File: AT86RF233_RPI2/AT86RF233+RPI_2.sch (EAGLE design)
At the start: 6 parts, among them U1 ATZB-RF-233-1-C

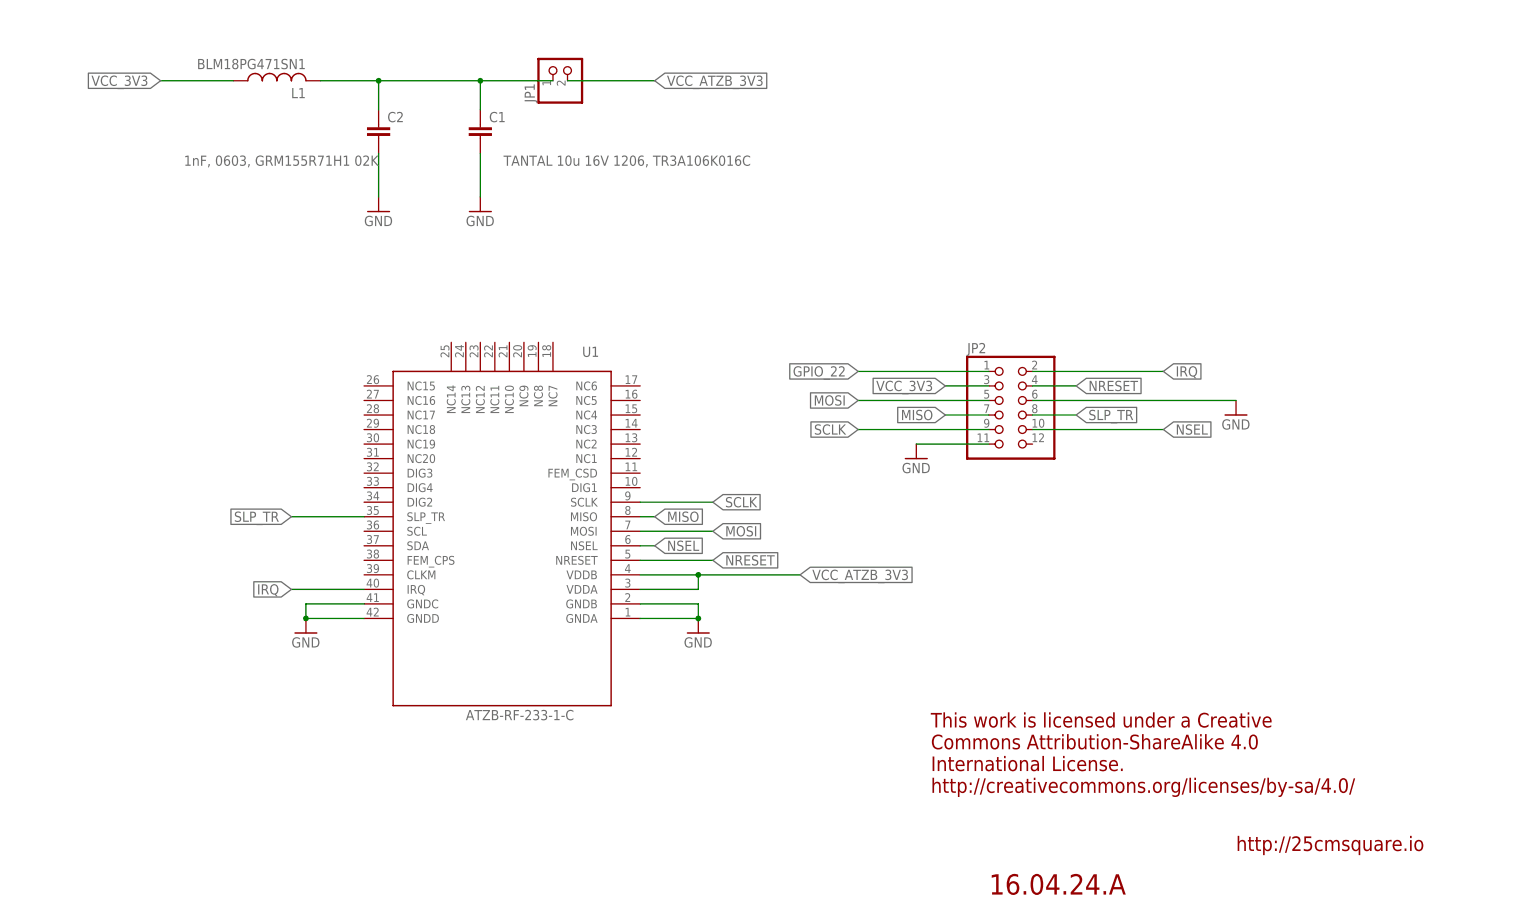
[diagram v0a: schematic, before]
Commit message: at86rf233: added reset switch
Signed-off-by: malo <malo@25cmsquare.io>
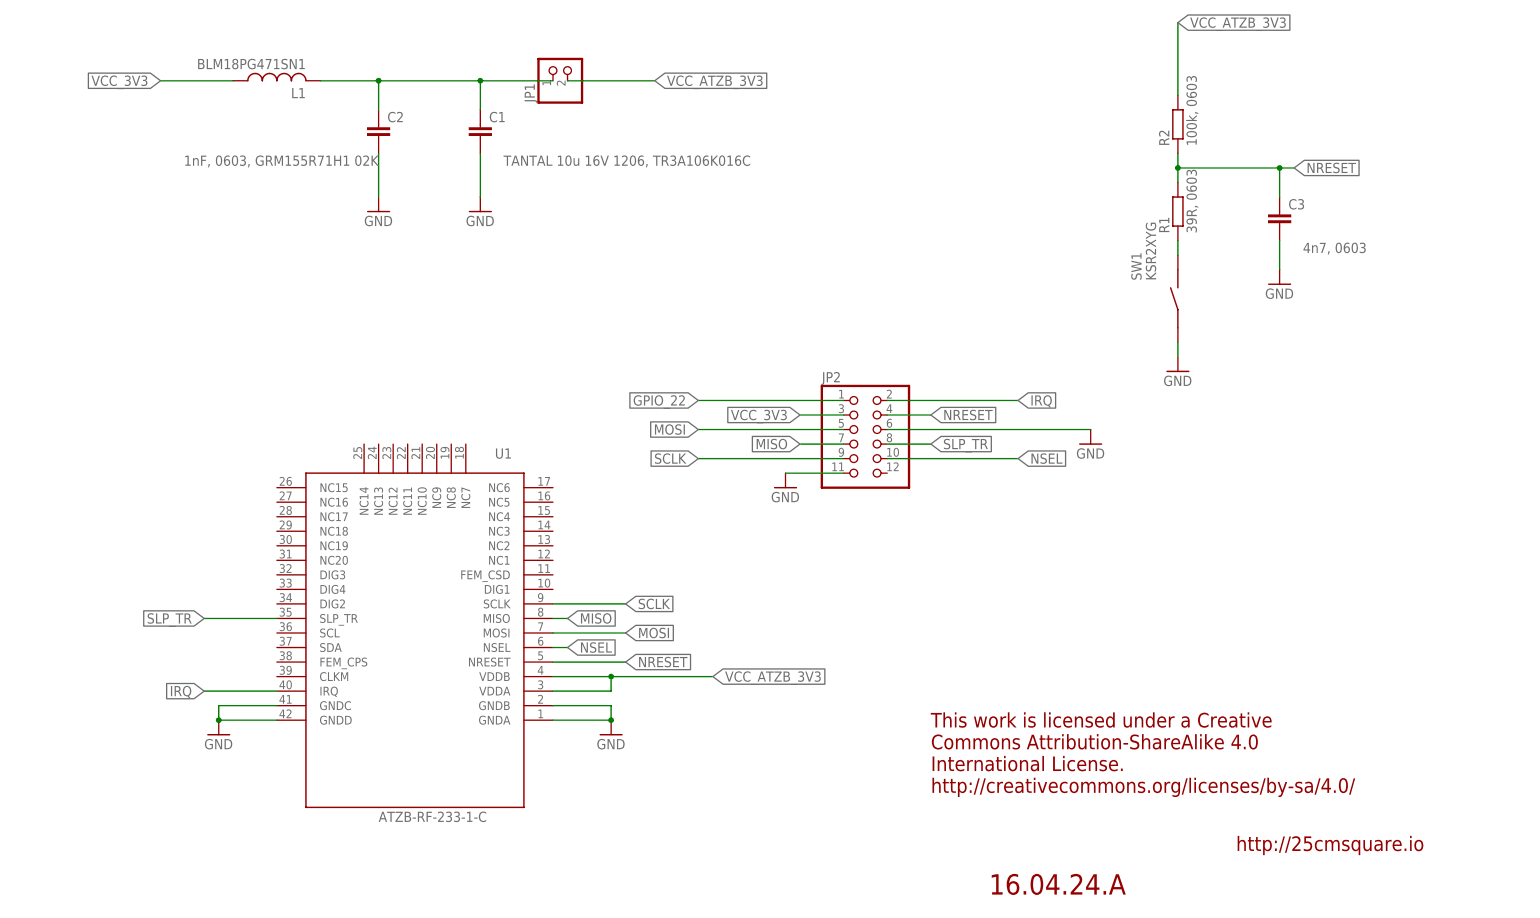
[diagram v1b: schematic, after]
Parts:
- added C3: 4n7, 0603, rcl:C-EUC0603K
- added R1: 39R, 0603, resistor:R-EU_R0603
- added R2: 100k, 0603, resistor:R-EU_R0603
- added SW1: KSR2XYG, 25cmsquare:KSR2XYG
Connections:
- new net N$1: R1.1, SW1.1
- net GND: now also C3.2, SW1.2
- net NRESET: now also C3.1, R1.2, R2.1
- net VCC_ATZB_3V3: now also R2.2
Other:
- moved on the sheet: JP2, U1

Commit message: at86rf233: board created
Signed-off-by: malo <malo@25cmsquare.io>
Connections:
- removed net N$2: C1.1, C2.1, JP1.1, L1.2
- new net N$3: JP1.2, L1.1
- net VCC_3V3: now also JP1.1; no longer L1.1
- net VCC_ATZB_3V3: now also C1.1, C2.1, L1.2; no longer JP1.2
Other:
- moved on the sheet: JP1
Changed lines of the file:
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@@
 <?xml version="1.0" encoding="utf-8"?>
 <!DOCTYPE eagle SYSTEM "eagle.dtd">
-<eagle version="7.2.0">
+<eagle version="7.5.0">
 <drawing>
 <settings>
@@
 </instance>
 <instance part="GND1" gate="1" x="83.82" y="132.08"/>
-<instance part="JP1" gate="G$1" x="99.06" y="157.48" rot="R90"/>
+<instance part="JP1" gate="G$1" x="27.94" y="157.48" rot="R90"/>
 <instance part="GND2" gate="1" x="38.1" y="40.64"/>
 <instance part="GND3" gate="1" x="106.68" y="40.64"/>
@@
 <net name="VCC_3V3" class="0">
 <segment>
-<pinref part="L1" gate="G$1" pin="1"/>
-<wire x1="40.64" y1="154.94" x2="27.94" y2="154.94" width="0.1524" layer="91"/>
-<label x="27.94" y="154.94" size="1.778" layer="95" rot="R180" xref="yes"/>
+<wire x1="25.4" y1="154.94" x2="17.78" y2="154.94" width="0.1524" layer="91"/>
+<label x="17.78" y="154.94" size="1.778" layer="95" rot="R180" xref="yes"/>
+<pinref part="JP1" gate="G$1" pin="1"/>
 </segment>
 <segment>
@@
 </segment>
 </net>
-<net name="N$2" class="0">
-<segment>
+<net name="VCC_ATZB_3V3" class="0">
+<segment>
+<label x="114.3" y="154.94" size="1.778" layer="95" xref="yes"/>
 <pinref part="L1" gate="G$1" pin="2"/>
-<pinref part="JP1" gate="G$1" pin="1"/>
 <wire x1="55.88" y1="154.94" x2="66.04" y2="154.94" width="0.1524" layer="91"/>
 <pinref part="C2" gate="G$1" pin="1"/>
 <wire x1="66.04" y1="154.94" x2="83.82" y2="154.94" width="0.1524" layer="91"/>
-<wire x1="83.82" y1="154.94" x2="96.52" y2="154.94" width="0.1524" layer="91"/>
 <wire x1="66.04" y1="149.86" x2="66.04" y2="154.94" width="0.1524" layer="91"/>
 <junction x="66.04" y="154.94"/>
 <pinref part="C1" gate="G$1" pin="1"/>
 <wire x1="83.82" y1="149.86" x2="83.82" y2="154.94" width="0.1524" layer="91"/>
+<wire x1="83.82" y1="154.94" x2="114.3" y2="154.94" width="0.1524" layer="91"/>
 <junction x="83.82" y="154.94"/>
-</segment>
-</net>
-<net name="VCC_ATZB_3V3" class="0">
-<segment>
-<pinref part="JP1" gate="G$1" pin="2"/>
-<wire x1="99.06" y1="154.94" x2="114.3" y2="154.94" width="0.1524" layer="91"/>
-<label x="114.3" y="154.94" size="1.778" layer="95" xref="yes"/>
 </segment>
 <segment>
@@
 </segment>
 </net>
+<net name="N$3" class="0">
+<segment>
+<pinref part="JP1" gate="G$1" pin="2"/>
+<pinref part="L1" gate="G$1" pin="1"/>
+<wire x1="27.94" y1="154.94" x2="40.64" y2="154.94" width="0.1524" layer="91"/>
+</segment>
+</net>
